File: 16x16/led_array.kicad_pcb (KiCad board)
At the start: 2 copper layers, 113.8 x 126.8 mm, 154 parts, among them M1 P***, M2 P***, M3 P***, M4 P***, P1 CONN_2, SW1 SWITCH_INV

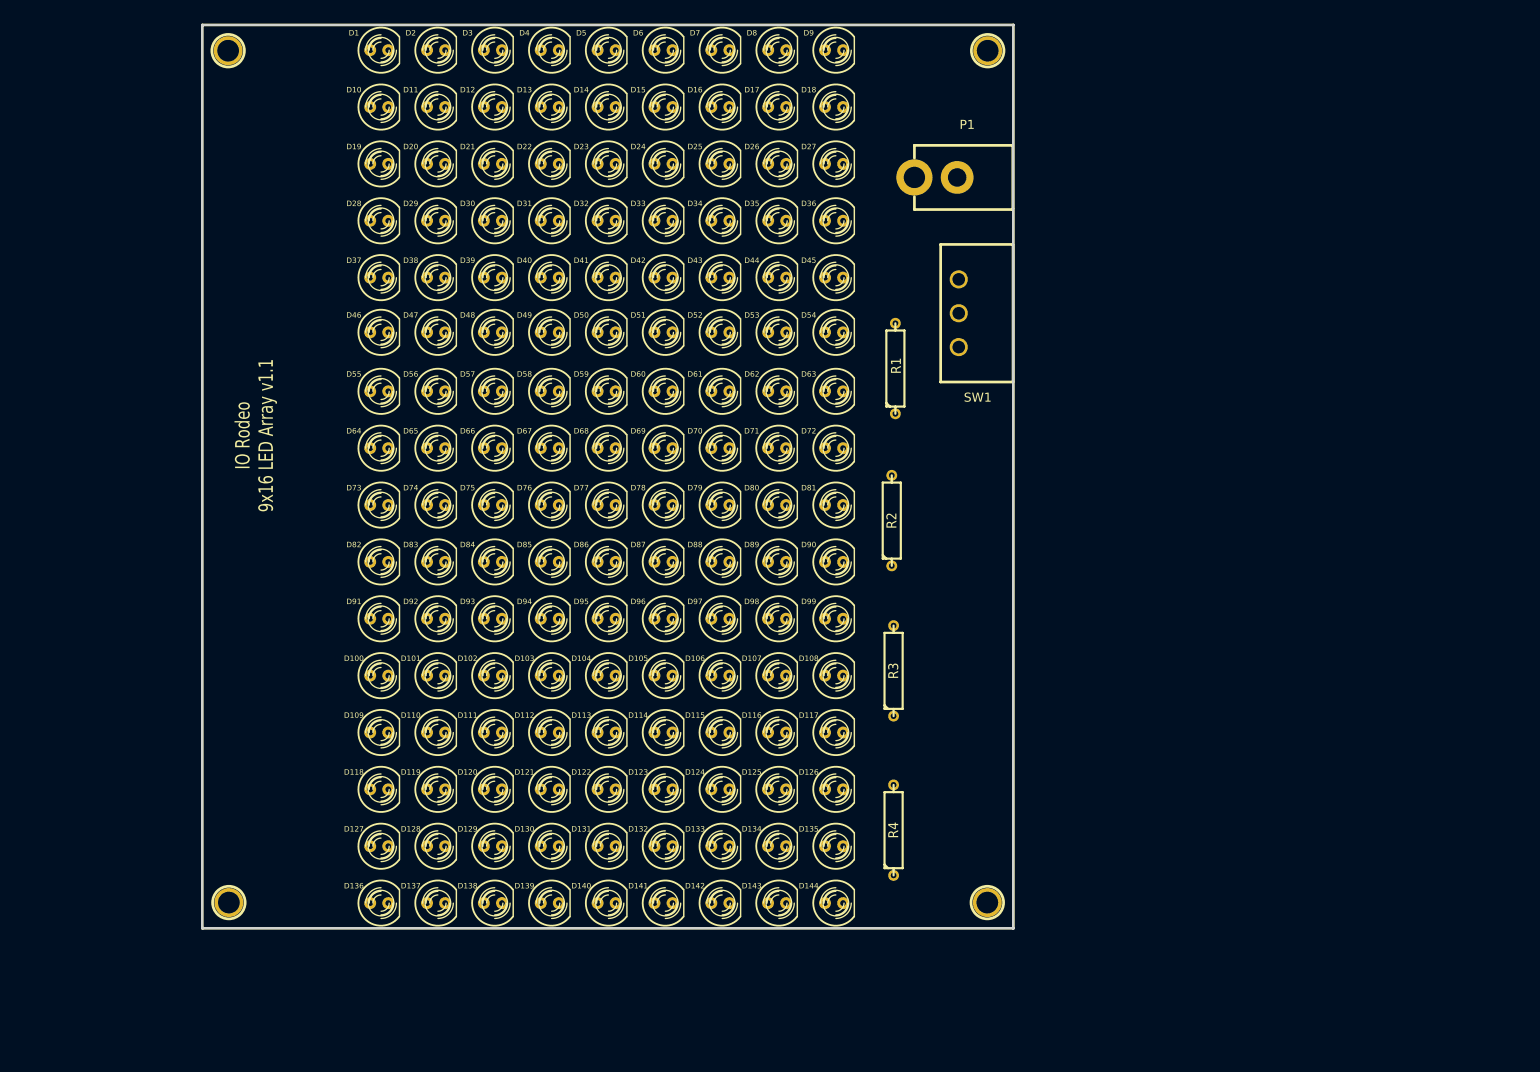
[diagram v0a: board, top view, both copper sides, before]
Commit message: Layout of additioanl LEDs in the 18x18 array.
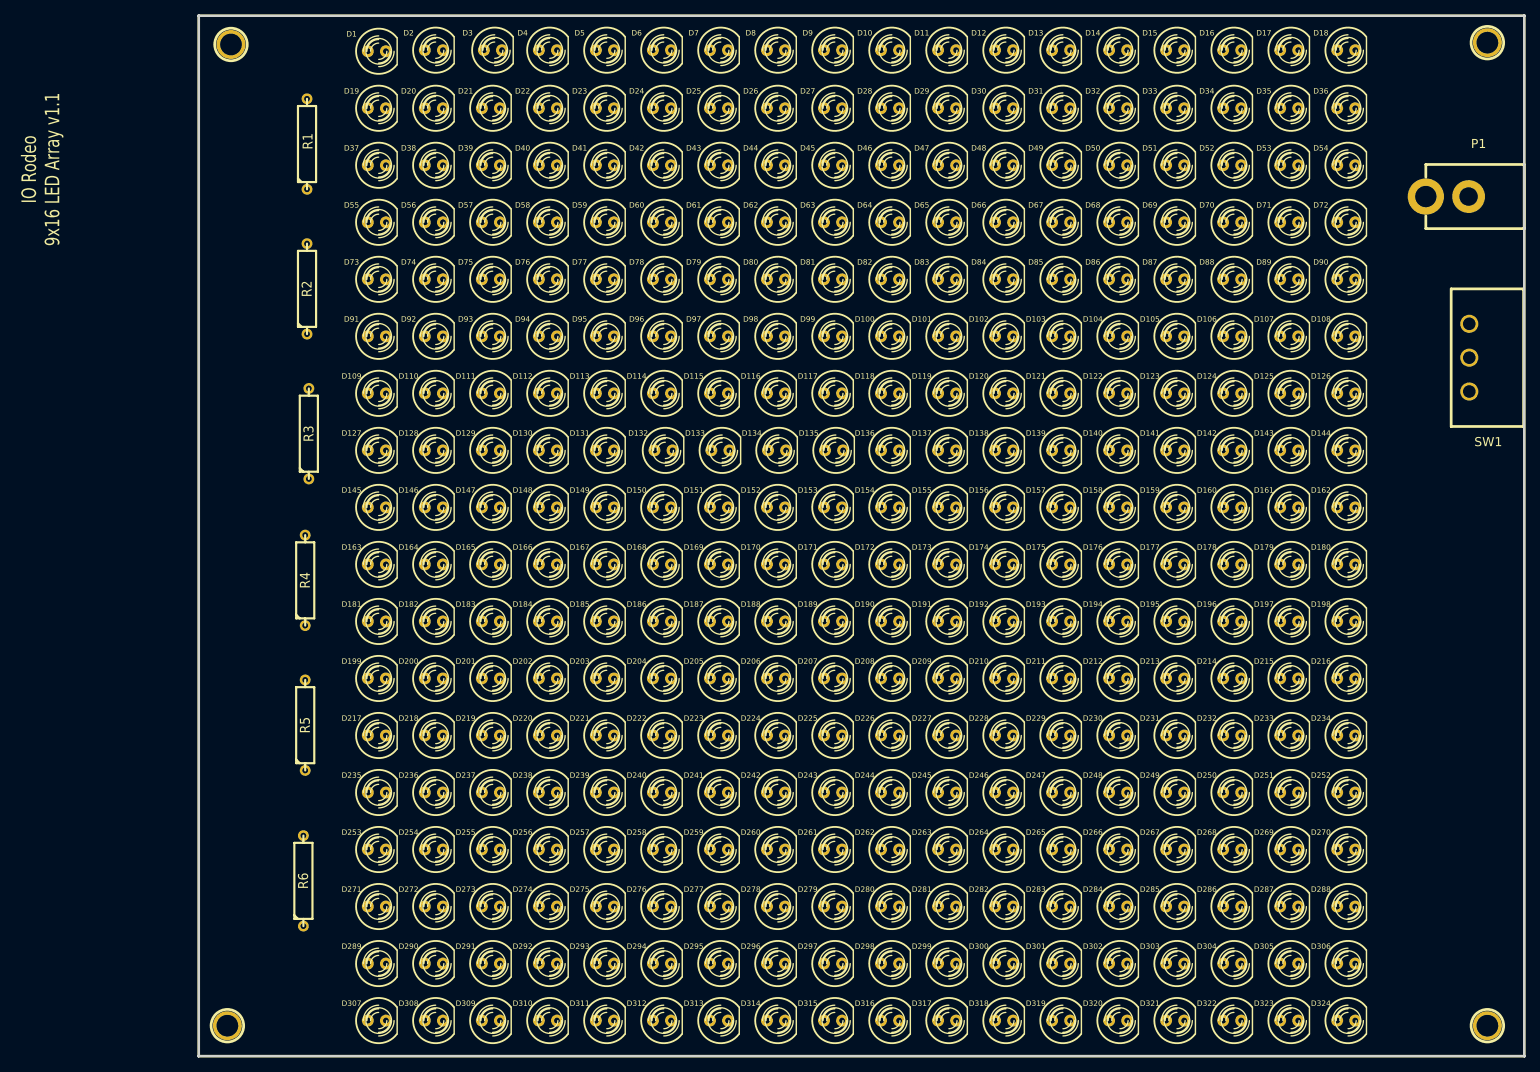
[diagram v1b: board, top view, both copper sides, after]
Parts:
- added D145: LED, CUSTOM2 LED-5MM, F.Cu at (86.0, 84.0)
- added D146: LED, CUSTOM2 LED-5MM, F.Cu at (94.0, 84.0)
- added D147: LED, CUSTOM2 LED-5MM, F.Cu at (102.0, 84.0)
- added D148: LED, CUSTOM2 LED-5MM, F.Cu at (110.0, 84.0)
- added D149: LED, CUSTOM2 LED-5MM, F.Cu at (118.0, 84.0)
- added D150: LED, CUSTOM2 LED-5MM, F.Cu at (126.0, 84.0)
- added D151: LED, CUSTOM2 LED-5MM, F.Cu at (134.0, 84.0)
- added D152: LED, CUSTOM2 LED-5MM, F.Cu at (142.0, 84.0)
- added D153: LED, CUSTOM2 LED-5MM, F.Cu at (150.0, 84.0)
- added D154: LED, CUSTOM2 LED-5MM, F.Cu at (158.0, 84.0)
- added D155: LED, CUSTOM2 LED-5MM, F.Cu at (166.0, 84.0)
- added D156: LED, CUSTOM2 LED-5MM, F.Cu at (174.0, 84.0)
- added D157: LED, CUSTOM2 LED-5MM, F.Cu at (182.0, 84.0)
- added D158: LED, CUSTOM2 LED-5MM, F.Cu at (190.0, 84.0)
- added D159: LED, CUSTOM2 LED-5MM, F.Cu at (198.0, 84.0)
- added D160: LED, CUSTOM2 LED-5MM, F.Cu at (206.0, 84.0)
- added D161: LED, CUSTOM2 LED-5MM, F.Cu at (214.0, 84.0)
- added D162: LED, CUSTOM2 LED-5MM, F.Cu at (222.0, 84.0)
- added D163: LED, CUSTOM2 LED-5MM, F.Cu at (86.0, 92.0)
- added D164: LED, CUSTOM2 LED-5MM, F.Cu at (94.0, 92.0)
- added D165: LED, CUSTOM2 LED-5MM, F.Cu at (102.0, 92.0)
- added D166: LED, CUSTOM2 LED-5MM, F.Cu at (110.0, 92.0)
- added D167: LED, CUSTOM2 LED-5MM, F.Cu at (118.0, 92.0)
- added D168: LED, CUSTOM2 LED-5MM, F.Cu at (126.0, 92.0)
- added D169: LED, CUSTOM2 LED-5MM, F.Cu at (134.0, 92.0)
- added D170: LED, CUSTOM2 LED-5MM, F.Cu at (142.0, 92.0)
- added D171: LED, CUSTOM2 LED-5MM, F.Cu at (150.0, 92.0)
- added D172: LED, CUSTOM2 LED-5MM, F.Cu at (158.0, 92.0)
- added D173: LED, CUSTOM2 LED-5MM, F.Cu at (166.0, 92.0)
- added D174: LED, CUSTOM2 LED-5MM, F.Cu at (174.0, 92.0)
- added D175: LED, CUSTOM2 LED-5MM, F.Cu at (182.0, 92.0)
- added D176: LED, CUSTOM2 LED-5MM, F.Cu at (190.0, 92.0)
- added D177: LED, CUSTOM2 LED-5MM, F.Cu at (198.0, 92.0)
- added D178: LED, CUSTOM2 LED-5MM, F.Cu at (206.0, 92.0)
- added D179: LED, CUSTOM2 LED-5MM, F.Cu at (214.0, 92.0)
- added D180: LED, CUSTOM2 LED-5MM, F.Cu at (222.0, 92.0)
- added D181: LED, CUSTOM2 LED-5MM, F.Cu at (86.0, 100.0)
- added D182: LED, CUSTOM2 LED-5MM, F.Cu at (94.0, 100.0)
- added D183: LED, CUSTOM2 LED-5MM, F.Cu at (102.0, 100.0)
- added D184: LED, CUSTOM2 LED-5MM, F.Cu at (110.0, 100.0)
- added D185: LED, CUSTOM2 LED-5MM, F.Cu at (118.0, 100.0)
- added D186: LED, CUSTOM2 LED-5MM, F.Cu at (126.0, 100.0)
- added D187: LED, CUSTOM2 LED-5MM, F.Cu at (134.0, 100.0)
- added D188: LED, CUSTOM2 LED-5MM, F.Cu at (142.0, 100.0)
- added D189: LED, CUSTOM2 LED-5MM, F.Cu at (150.0, 100.0)
- added D190: LED, CUSTOM2 LED-5MM, F.Cu at (158.0, 100.0)
- added D191: LED, CUSTOM2 LED-5MM, F.Cu at (166.0, 100.0)
- added D192: LED, CUSTOM2 LED-5MM, F.Cu at (174.0, 100.0)
- added D193: LED, CUSTOM2 LED-5MM, F.Cu at (182.0, 100.0)
- added D194: LED, CUSTOM2 LED-5MM, F.Cu at (190.0, 100.0)
- added D195: LED, CUSTOM2 LED-5MM, F.Cu at (198.0, 100.0)
- added D196: LED, CUSTOM2 LED-5MM, F.Cu at (206.0, 100.0)
- added D197: LED, CUSTOM2 LED-5MM, F.Cu at (214.0, 100.0)
- added D198: LED, CUSTOM2 LED-5MM, F.Cu at (222.0, 100.0)
- added D199: LED, CUSTOM2 LED-5MM, F.Cu at (86.0, 108.0)
- added D200: LED, CUSTOM2 LED-5MM, F.Cu at (94.0, 108.0)
- added D201: LED, CUSTOM2 LED-5MM, F.Cu at (102.0, 108.0)
- added D202: LED, CUSTOM2 LED-5MM, F.Cu at (110.0, 108.0)
- added D203: LED, CUSTOM2 LED-5MM, F.Cu at (118.0, 108.0)
- added D204: LED, CUSTOM2 LED-5MM, F.Cu at (126.0, 108.0)
- added D205: LED, CUSTOM2 LED-5MM, F.Cu at (134.0, 108.0)
- added D206: LED, CUSTOM2 LED-5MM, F.Cu at (142.0, 108.0)
- added D207: LED, CUSTOM2 LED-5MM, F.Cu at (150.0, 108.0)
- added D208: LED, CUSTOM2 LED-5MM, F.Cu at (158.0, 108.0)
- added D209: LED, CUSTOM2 LED-5MM, F.Cu at (166.0, 108.0)
- added D210: LED, CUSTOM2 LED-5MM, F.Cu at (174.0, 108.0)
- added D211: LED, CUSTOM2 LED-5MM, F.Cu at (182.0, 108.0)
- added D212: LED, CUSTOM2 LED-5MM, F.Cu at (190.0, 108.0)
- added D213: LED, CUSTOM2 LED-5MM, F.Cu at (198.0, 108.0)
- added D214: LED, CUSTOM2 LED-5MM, F.Cu at (206.0, 108.0)
- added D215: LED, CUSTOM2 LED-5MM, F.Cu at (214.0, 108.0)
- added D216: LED, CUSTOM2 LED-5MM, F.Cu at (222.0, 108.0)
- added D217: LED, CUSTOM2 LED-5MM, F.Cu at (86.0, 116.0)
- added D218: LED, CUSTOM2 LED-5MM, F.Cu at (94.0, 116.0)
- added D219: LED, CUSTOM2 LED-5MM, F.Cu at (102.0, 116.0)
- added D220: LED, CUSTOM2 LED-5MM, F.Cu at (110.0, 116.0)
- added D221: LED, CUSTOM2 LED-5MM, F.Cu at (118.0, 116.0)
- added D222: LED, CUSTOM2 LED-5MM, F.Cu at (126.0, 116.0)
- added D223: LED, CUSTOM2 LED-5MM, F.Cu at (134.0, 116.0)
- added D224: LED, CUSTOM2 LED-5MM, F.Cu at (142.0, 116.0)
- added D225: LED, CUSTOM2 LED-5MM, F.Cu at (150.0, 116.0)
- added D226: LED, CUSTOM2 LED-5MM, F.Cu at (158.0, 116.0)
- added D227: LED, CUSTOM2 LED-5MM, F.Cu at (166.0, 116.0)
- added D228: LED, CUSTOM2 LED-5MM, F.Cu at (174.0, 116.0)
- added D229: LED, CUSTOM2 LED-5MM, F.Cu at (182.0, 116.0)
- added D230: LED, CUSTOM2 LED-5MM, F.Cu at (190.0, 116.0)
- added D231: LED, CUSTOM2 LED-5MM, F.Cu at (198.0, 116.0)
- added D232: LED, CUSTOM2 LED-5MM, F.Cu at (206.0, 116.0)
- added D233: LED, CUSTOM2 LED-5MM, F.Cu at (214.0, 116.0)
- added D234: LED, CUSTOM2 LED-5MM, F.Cu at (222.0, 116.0)
- added D235: LED, CUSTOM2 LED-5MM, F.Cu at (86.0, 124.0)
- added D236: LED, CUSTOM2 LED-5MM, F.Cu at (94.0, 124.0)
- added D237: LED, CUSTOM2 LED-5MM, F.Cu at (102.0, 124.0)
- added D238: LED, CUSTOM2 LED-5MM, F.Cu at (110.0, 124.0)
- added D239: LED, CUSTOM2 LED-5MM, F.Cu at (118.0, 124.0)
- added D240: LED, CUSTOM2 LED-5MM, F.Cu at (126.0, 124.0)
- added D241: LED, CUSTOM2 LED-5MM, F.Cu at (134.0, 124.0)
- added D242: LED, CUSTOM2 LED-5MM, F.Cu at (142.0, 124.0)
- added D243: LED, CUSTOM2 LED-5MM, F.Cu at (150.0, 124.0)
- added D244: LED, CUSTOM2 LED-5MM, F.Cu at (158.0, 124.0)
- added D245: LED, CUSTOM2 LED-5MM, F.Cu at (166.0, 124.0)
- added D246: LED, CUSTOM2 LED-5MM, F.Cu at (174.0, 124.0)
- added D247: LED, CUSTOM2 LED-5MM, F.Cu at (182.0, 124.0)
- added D248: LED, CUSTOM2 LED-5MM, F.Cu at (190.0, 124.0)
- added D249: LED, CUSTOM2 LED-5MM, F.Cu at (198.0, 124.0)
- added D250: LED, CUSTOM2 LED-5MM, F.Cu at (206.0, 124.0)
- added D251: LED, CUSTOM2 LED-5MM, F.Cu at (214.0, 124.0)
- added D252: LED, CUSTOM2 LED-5MM, F.Cu at (222.0, 124.0)
- added D253: LED, CUSTOM2 LED-5MM, F.Cu at (86.0, 132.0)
- added D254: LED, CUSTOM2 LED-5MM, F.Cu at (94.0, 132.0)
- added D255: LED, CUSTOM2 LED-5MM, F.Cu at (102.0, 132.0)
- added D256: LED, CUSTOM2 LED-5MM, F.Cu at (110.0, 132.0)
- added D257: LED, CUSTOM2 LED-5MM, F.Cu at (118.0, 132.0)
- added D258: LED, CUSTOM2 LED-5MM, F.Cu at (126.0, 132.0)
- added D259: LED, CUSTOM2 LED-5MM, F.Cu at (134.0, 132.0)
- added D260: LED, CUSTOM2 LED-5MM, F.Cu at (142.0, 132.0)
- added D261: LED, CUSTOM2 LED-5MM, F.Cu at (150.0, 132.0)
- added D262: LED, CUSTOM2 LED-5MM, F.Cu at (158.0, 132.0)
- added D263: LED, CUSTOM2 LED-5MM, F.Cu at (166.0, 132.0)
- added D264: LED, CUSTOM2 LED-5MM, F.Cu at (174.0, 132.0)
- added D265: LED, CUSTOM2 LED-5MM, F.Cu at (182.0, 132.0)
- added D266: LED, CUSTOM2 LED-5MM, F.Cu at (190.0, 132.0)
- added D267: LED, CUSTOM2 LED-5MM, F.Cu at (198.0, 132.0)
- added D268: LED, CUSTOM2 LED-5MM, F.Cu at (206.0, 132.0)
- added D269: LED, CUSTOM2 LED-5MM, F.Cu at (214.0, 132.0)
- added D270: LED, CUSTOM2 LED-5MM, F.Cu at (222.0, 132.0)
- added D271: LED, CUSTOM2 LED-5MM, F.Cu at (86.0, 140.0)
- added D272: LED, CUSTOM2 LED-5MM, F.Cu at (94.0, 140.0)
- added D273: LED, CUSTOM2 LED-5MM, F.Cu at (102.0, 140.0)
- added D274: LED, CUSTOM2 LED-5MM, F.Cu at (110.0, 140.0)
- added D275: LED, CUSTOM2 LED-5MM, F.Cu at (118.0, 140.0)
- added D276: LED, CUSTOM2 LED-5MM, F.Cu at (126.0, 140.0)
- added D277: LED, CUSTOM2 LED-5MM, F.Cu at (134.0, 140.0)
- added D278: LED, CUSTOM2 LED-5MM, F.Cu at (142.0, 140.0)
- added D279: LED, CUSTOM2 LED-5MM, F.Cu at (150.0, 140.0)
- added D280: LED, CUSTOM2 LED-5MM, F.Cu at (158.0, 140.0)
- added D281: LED, CUSTOM2 LED-5MM, F.Cu at (166.0, 140.0)
- added D282: LED, CUSTOM2 LED-5MM, F.Cu at (174.0, 140.0)
- added D283: LED, CUSTOM2 LED-5MM, F.Cu at (182.0, 140.0)
- added D284: LED, CUSTOM2 LED-5MM, F.Cu at (190.0, 140.0)
- added D285: LED, CUSTOM2 LED-5MM, F.Cu at (198.0, 140.0)
- added D286: LED, CUSTOM2 LED-5MM, F.Cu at (206.0, 140.0)
- added D287: LED, CUSTOM2 LED-5MM, F.Cu at (214.0, 140.0)
- added D288: LED, CUSTOM2 LED-5MM, F.Cu at (222.0, 140.0)
- added D289: LED, CUSTOM2 LED-5MM, F.Cu at (86.0, 148.0)
- added D290: LED, CUSTOM2 LED-5MM, F.Cu at (94.0, 148.0)
- added D291: LED, CUSTOM2 LED-5MM, F.Cu at (102.0, 148.0)
- added D292: LED, CUSTOM2 LED-5MM, F.Cu at (110.0, 148.0)
- added D293: LED, CUSTOM2 LED-5MM, F.Cu at (118.0, 148.0)
- added D294: LED, CUSTOM2 LED-5MM, F.Cu at (126.0, 148.0)
- added D295: LED, CUSTOM2 LED-5MM, F.Cu at (134.0, 148.0)
- added D296: LED, CUSTOM2 LED-5MM, F.Cu at (142.0, 148.0)
- added D297: LED, CUSTOM2 LED-5MM, F.Cu at (150.0, 148.0)
- added D298: LED, CUSTOM2 LED-5MM, F.Cu at (158.0, 148.0)
- added D299: LED, CUSTOM2 LED-5MM, F.Cu at (166.0, 148.0)
- added D300: LED, CUSTOM2 LED-5MM, F.Cu at (174.0, 148.0)
- added D301: LED, CUSTOM2 LED-5MM, F.Cu at (182.0, 148.0)
- added D302: LED, CUSTOM2 LED-5MM, F.Cu at (190.0, 148.0)
- added D303: LED, CUSTOM2 LED-5MM, F.Cu at (198.0, 148.0)
- added D304: LED, CUSTOM2 LED-5MM, F.Cu at (206.0, 148.0)
- added D305: LED, CUSTOM2 LED-5MM, F.Cu at (214.0, 148.0)
- added D306: LED, CUSTOM2 LED-5MM, F.Cu at (222.0, 148.0)
- added D307: LED, CUSTOM2 LED-5MM, F.Cu at (86.0, 156.0)
- added D308: LED, CUSTOM2 LED-5MM, F.Cu at (94.0, 156.0)
- added D309: LED, CUSTOM2 LED-5MM, F.Cu at (102.0, 156.0)
- added D310: LED, CUSTOM2 LED-5MM, F.Cu at (110.0, 156.0)
- added D311: LED, CUSTOM2 LED-5MM, F.Cu at (118.0, 156.0)
- added D312: LED, CUSTOM2 LED-5MM, F.Cu at (126.0, 156.0)
- added D313: LED, CUSTOM2 LED-5MM, F.Cu at (134.0, 156.0)
- added D314: LED, CUSTOM2 LED-5MM, F.Cu at (142.0, 156.0)
- added D315: LED, CUSTOM2 LED-5MM, F.Cu at (150.0, 156.0)
- added D316: LED, CUSTOM2 LED-5MM, F.Cu at (158.0, 156.0)
- added D317: LED, CUSTOM2 LED-5MM, F.Cu at (166.0, 156.0)
- added D318: LED, CUSTOM2 LED-5MM, F.Cu at (174.0, 156.0)
- added D319: LED, CUSTOM2 LED-5MM, F.Cu at (182.0, 156.0)
- added D320: LED, CUSTOM2 LED-5MM, F.Cu at (190.0, 156.0)
- added D321: LED, CUSTOM2 LED-5MM, F.Cu at (198.0, 156.0)
- added D322: LED, CUSTOM2 LED-5MM, F.Cu at (206.0, 156.0)
- added D323: LED, CUSTOM2 LED-5MM, F.Cu at (214.0, 156.0)
- added D324: LED, CUSTOM2 LED-5MM, F.Cu at (222.0, 156.0)
- added R5: R, R5, F.Cu at (75.9, 114.6)
- added R6: R, R5, F.Cu at (75.7, 136.4)
- moved M2 153.7 mm to (241.8, 156.7)
- moved M3 139.6 mm to (241.8, 18.8)
- moved D144 95.9 mm to (222.0, 76.0)
- moved D143 95.9 mm to (214.0, 76.0)
- moved D142 95.9 mm to (206.0, 76.0)
- moved D141 95.9 mm to (198.0, 76.0)
- moved D140 95.8 mm to (190.0, 76.0)
- moved D139 95.8 mm to (182.0, 76.0)
- moved D138 95.8 mm to (174.0, 76.0)
- moved D137 95.8 mm to (166.0, 76.0)
- moved D136 95.8 mm to (158.0, 76.0)
- moved D126 90.8 mm to (222.0, 68.0)
- moved D125 90.8 mm to (214.0, 68.0)
- moved D124 90.8 mm to (206.0, 68.0)
- moved D123 90.8 mm to (198.0, 68.0)
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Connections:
- D1 pad 1: N-0000032 -> N-00000254
- D100 pad 2: N-0000031 -> N-00000162
- D101 pad 1: N-0000032 -> N-00000162
- D102 pad 2: N-0000010 -> N-00000257
- D103 pad 1: N-0000010 -> N-00000254
- D104 pad 2: N-0000031 -> N-00000175
- D105 pad 1: N-0000032 -> N-00000175
- D108 pad 2: N-0000031 -> N-00000257
- D109 pad 1: N-0000032 -> N-00000254
- D112 pad 2: N-0000029 -> N-00000224
- D113 pad 1: N-0000032 -> N-00000224
- D114 pad 2: N-0000075 -> N-00000249
- D115 pad 1: N-0000075 -> N-00000254
- D116 pad 2: N-0000029 -> N-00000220
- D117 pad 1: N-0000032 -> N-00000220
- D12 pad 2: N-000005 -> N-00000197
- D120 pad 2: N-0000029 -> N-00000249
- D121 pad 1: N-0000032 -> N-00000254
- D124 pad 2: N-0000029 -> N-00000214
- D125 pad 1: N-0000032 -> N-00000214
- D126 pad 2: N-0000089 -> N-00000249
- D127 pad 1: N-0000089 -> N-00000254
- D128 pad 2: N-0000029 -> N-00000217
- D129 pad 1: N-0000032 -> N-00000217
- D13 pad 1: N-0000032 -> N-00000254
- D132 pad 2: N-0000029 -> N-00000249
- D133 pad 1: N-0000032 -> N-00000254
- D136 pad 2: N-0000029 -> N-00000252
- D137 pad 1: N-0000032 -> N-00000252
- D138 pad 2: N-00000112 -> N-00000249
- D139 pad 1: N-00000112 -> N-00000254
- D140 pad 2: N-0000029 -> N-00000227
- D141 pad 1: N-0000032 -> N-00000227
- D144 pad 2: N-0000029 -> N-00000249
- D16 pad 2: N-000005 -> N-00000157
- D17 pad 1: N-0000032 -> N-00000157
- D18 pad 2: N-0000054 -> N-00000197
- D19 pad 1: N-0000054 -> N-00000254
- D20 pad 2: N-000005 -> N-00000206
- D21 pad 1: N-0000032 -> N-00000206
- D24 pad 2: N-000005 -> N-00000197
- D25 pad 1: N-0000032 -> N-00000254
- D28 pad 2: N-000005 -> N-00000150
- D29 pad 1: N-0000032 -> N-00000150
- D30 pad 2: N-0000048 -> N-00000197
- D31 pad 1: N-0000048 -> N-00000254
- D32 pad 2: N-000005 -> N-00000187
- D33 pad 1: N-0000032 -> N-00000187
- D36 pad 2: N-000005 -> N-00000197
- D37 pad 1: N-0000032 -> N-00000254
- D4 pad 2: N-000005 -> N-00000141
- D40 pad 2: N-000004 -> N-00000151
- D41 pad 1: N-0000032 -> N-00000151
- D42 pad 2: N-0000063 -> N-00000197
- D43 pad 1: N-0000063 -> N-00000254
- D44 pad 2: N-000004 -> N-00000190
- D45 pad 1: N-0000032 -> N-00000190
- D48 pad 2: N-000004 -> N-00000197
- D49 pad 1: N-0000032 -> N-00000254
- D5 pad 1: N-0000032 -> N-00000141
- D52 pad 2: N-000004 -> N-00000143
- D53 pad 1: N-0000032 -> N-00000143
- D54 pad 2: N-0000036 -> N-00000197
- D55 pad 1: N-0000036 -> N-00000254
- D56 pad 2: N-000004 -> N-00000267
- D57 pad 1: N-0000032 -> N-00000267
- D6 pad 2: N-0000099 -> N-00000197
- D60 pad 2: N-000004 -> N-00000257
- D61 pad 1: N-0000032 -> N-00000254
- D64 pad 2: N-000004 -> N-00000260
- D65 pad 1: N-0000032 -> N-00000260
- D66 pad 2: N-0000061 -> N-00000257
- D67 pad 1: N-0000061 -> N-00000254
- D68 pad 2: N-000004 -> N-00000168
- D69 pad 1: N-0000032 -> N-00000168
- D7 pad 1: N-0000099 -> N-00000254
- D72 pad 2: N-000004 -> N-00000257
- D73 pad 1: N-0000032 -> N-00000254
- D76 pad 2: N-0000031 -> N-00000172
- D77 pad 1: N-0000032 -> N-00000172
- D78 pad 2: N-0000021 -> N-00000257
- D79 pad 1: N-0000021 -> N-00000254
- D8 pad 2: N-000005 -> N-00000209
- D80 pad 2: N-0000031 -> N-00000179
- D81 pad 1: N-0000032 -> N-00000179
- D84 pad 2: N-0000031 -> N-00000257
- D85 pad 1: N-0000032 -> N-00000254
- D88 pad 2: N-0000031 -> N-00000183
- D89 pad 1: N-0000032 -> N-00000183
- D9 pad 1: N-0000032 -> N-00000209
- D90 pad 2: N-0000016 -> N-00000257
- D91 pad 1: N-0000016 -> N-00000254
- D92 pad 2: N-0000031 -> N-00000165
- D93 pad 1: N-0000032 -> N-00000165
- D96 pad 2: N-0000031 -> N-00000257
- D97 pad 1: N-0000032 -> N-00000254
- R1 pad 1: N-000005 -> N-00000197
- R2 pad 1: N-000004 -> N-00000257
- R3 pad 1: N-0000031 -> N-00000249
- R4 pad 1: N-0000029 -> N-0000061
- SW1 pad 2: N-0000032 -> N-00000254
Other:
- board size 113.8 x 126.8 mm -> 186 x 146 mm
